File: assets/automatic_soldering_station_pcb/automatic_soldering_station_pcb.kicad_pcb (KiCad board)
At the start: 2 copper layers, 118.5 x 94.5 mm, 30 parts, among them J1 XY_MOS, J2 MAX6675, J3 MAX6675, J4 MAX6675, J5 I2C_DATA_PORT

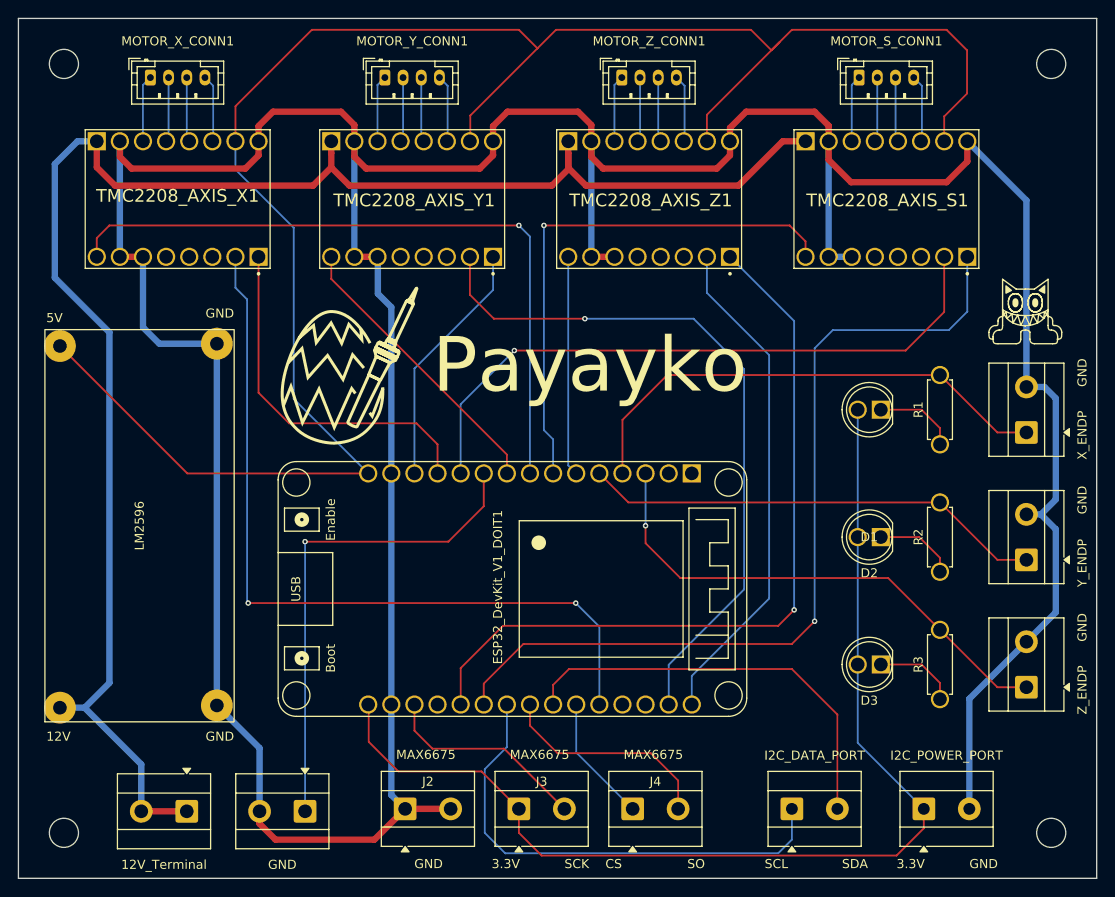
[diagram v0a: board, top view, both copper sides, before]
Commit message: pcb: add ground plane
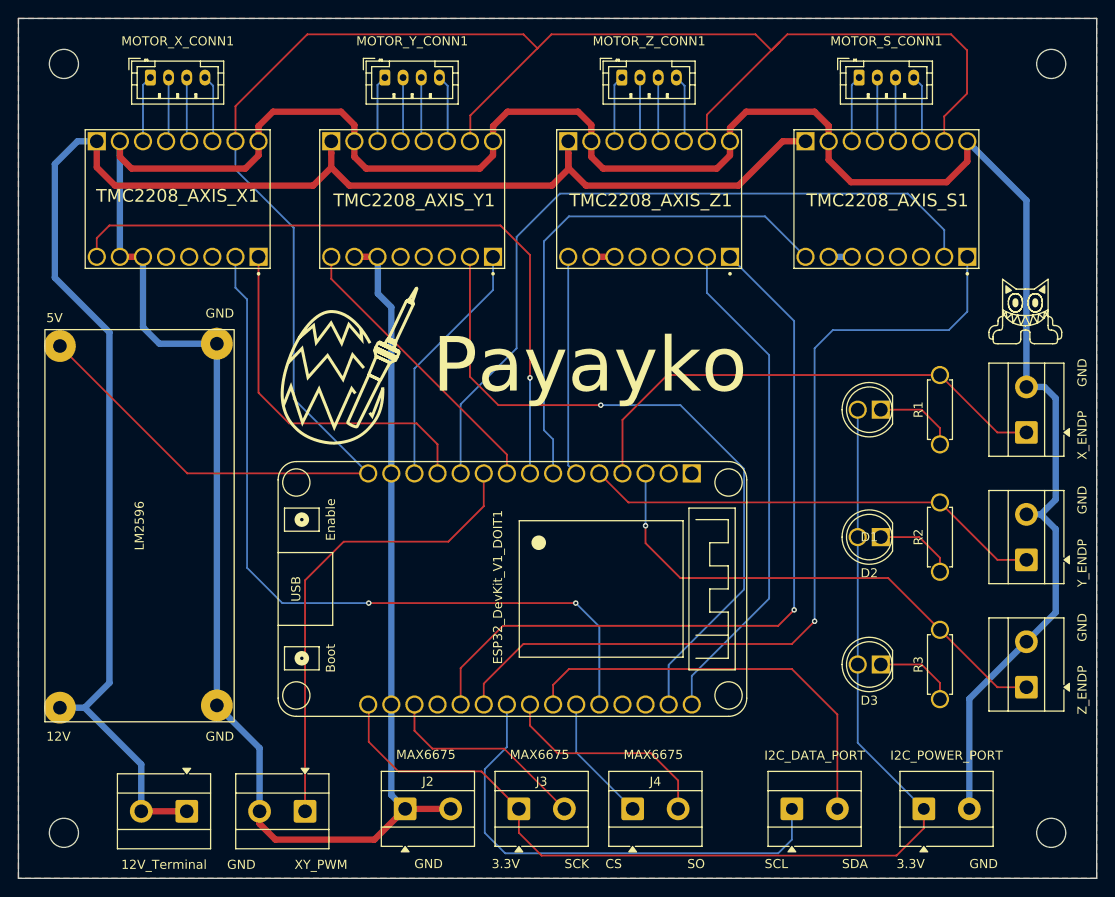
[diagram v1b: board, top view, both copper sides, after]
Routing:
- net GND: track 430.7 -> 392.6 mm
- net /S_STEP: track 71.0 -> 82.1 mm, vias 1 -> 0
- net /XY_MOS_PWM: track 54.5 -> 52.0 mm, vias 1 -> 0
- net /X_STEP: track 86.9 -> 84.7 mm
- net +5V: track 213.1 -> 211.8 mm
- net /S_EN: track 58.8 -> 57.7 mm, vias 1 -> 0
- net /X_EN: track 76.8 -> 75.6 mm
- net /Y_STEP: track 78.0 -> 76.8 mm
- added copper zone on B.Cu, net GND
- added copper zone on F.Cu, net GND
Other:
- board text added: "XY_PWM"
